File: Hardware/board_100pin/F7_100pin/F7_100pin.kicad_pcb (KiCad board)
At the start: 4 copper layers, 69.8 x 45.7 mm, 77 parts, among them IC1 OPA659IDBVR, IC2 OPA659IDBVR, IC3 LMH6643MAX_NOPB, IC4 TPS65133DPDR, J1 SMA Edge, J2 Pre-Amp, J3 UART, J4 5V, J5 Filter, J6 3V3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

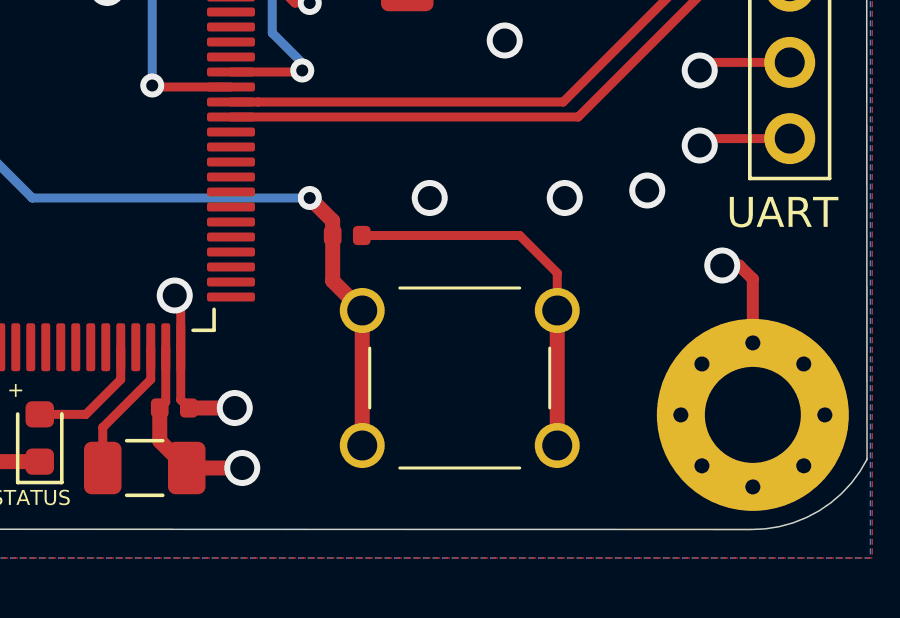
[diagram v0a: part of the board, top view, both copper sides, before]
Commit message: Updated F7 100 pin schematic
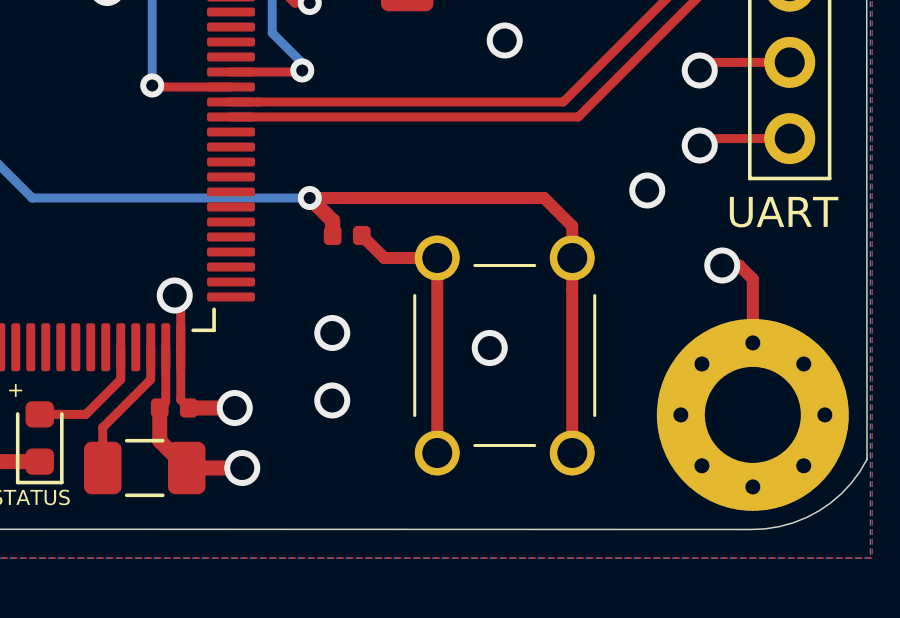
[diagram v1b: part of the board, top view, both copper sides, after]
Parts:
- moved S1 1.68 mm to (120.0, 60.2), turned to 90 degrees
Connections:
- S1 pad 2: GND -> NRST
- S1 pad 4: NRST -> GND
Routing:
- net NRST: track 62.4 -> 71.7 mm
- net GND: track 252.4 -> 248.9 mm, vias 79 -> 80

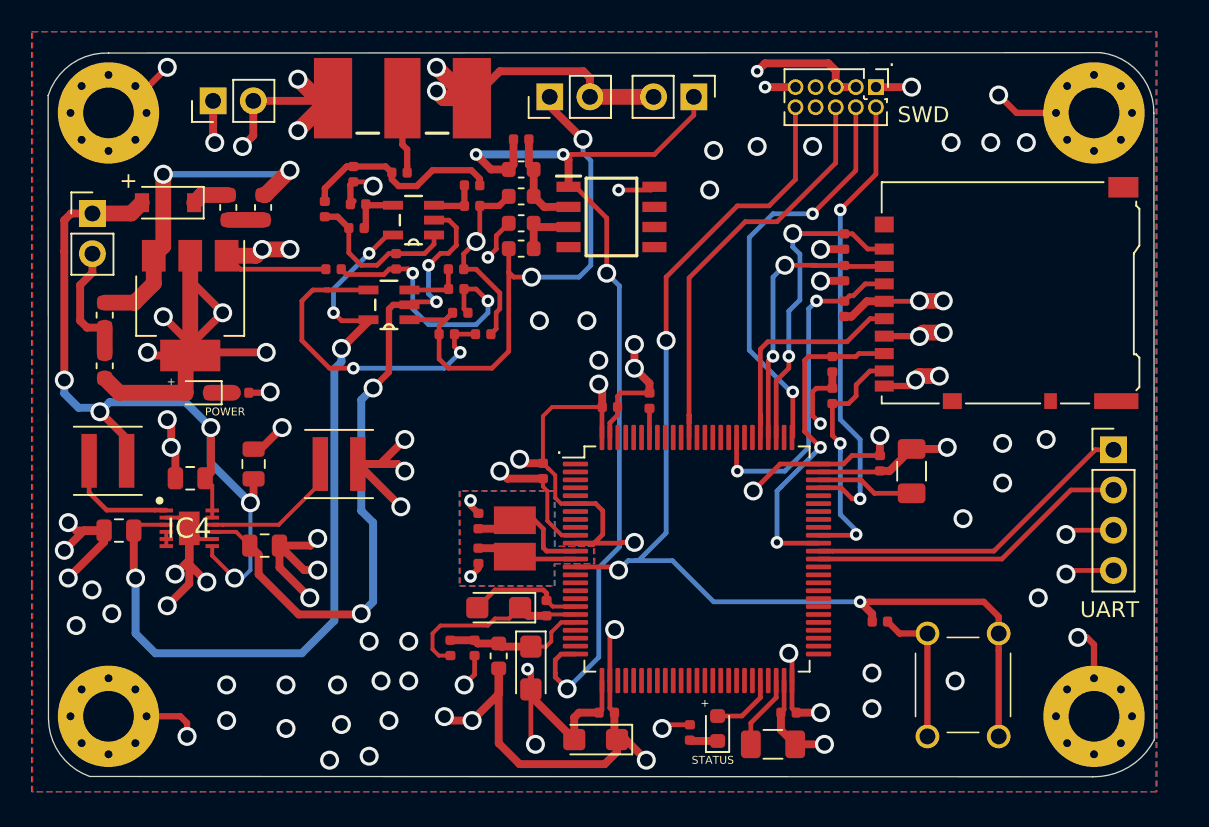
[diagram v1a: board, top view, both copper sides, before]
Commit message: Edited board to add USB power
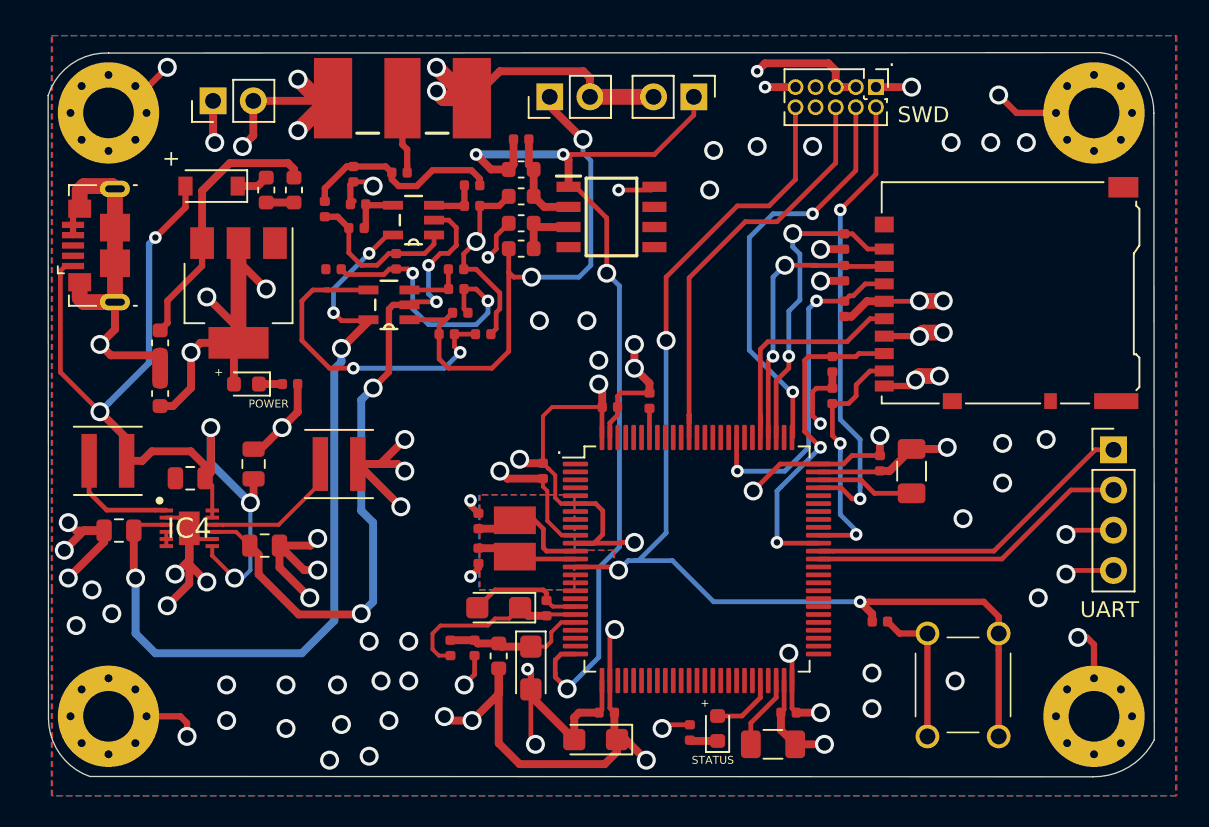
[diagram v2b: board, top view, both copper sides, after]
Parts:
- J4: value 5V -> USB_B_Micro; footprint Connector_PinHeader_2.54mm:PinHeader_1x02_P2.54mm_Vertical -> Connector_USB:USB_Micro-B_GCT_USB3076-30-A
- moved C10 3.91 mm to (69.3, 38.6)
- moved C11 3.91 mm to (69.3, 41.9)
- moved U1 3.15 mm to (74.2, 35.5)
- moved R24 3.13 mm to (77.5, 41.2)
- moved D4 3.10 mm to (74.8, 41.2)
- moved D1 2.94 mm to (72.5, 28.8)
- moved F1 2.64 mm to (76.0, 29.0)
- moved FB1 2.24 mm to (77.8, 29.0)
- moved J4 2.03 mm to (65.2, 32.5), turned to 90 degrees
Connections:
- J4 pad 2: GND -> Net-(J4-Pad2)
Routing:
- net 3V3: track 172.7 -> 154.2 mm, vias 26 -> 25
- net VCC: track 52.2 -> 59.0 mm
- net Net-(C10-Pad1): track 21.3 -> 17.1 mm, vias 2 -> 0
- net GND: track 248.9 -> 252.8 mm, vias 80 -> 76
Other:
- board text removed: "VCC"
